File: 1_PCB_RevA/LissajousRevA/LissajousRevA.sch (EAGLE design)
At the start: 77 parts, among them U101 LM348D, U201 LM348D, U401 LM348D

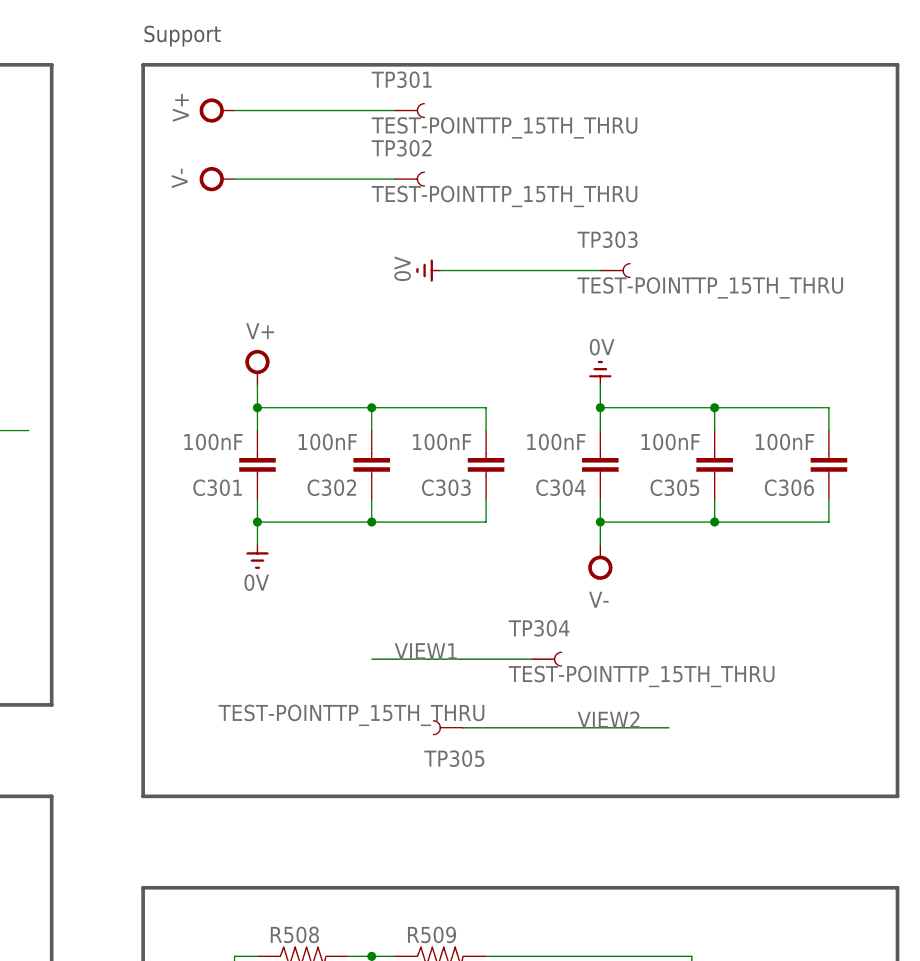
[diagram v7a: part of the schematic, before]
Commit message: added bigger test pads to pcb
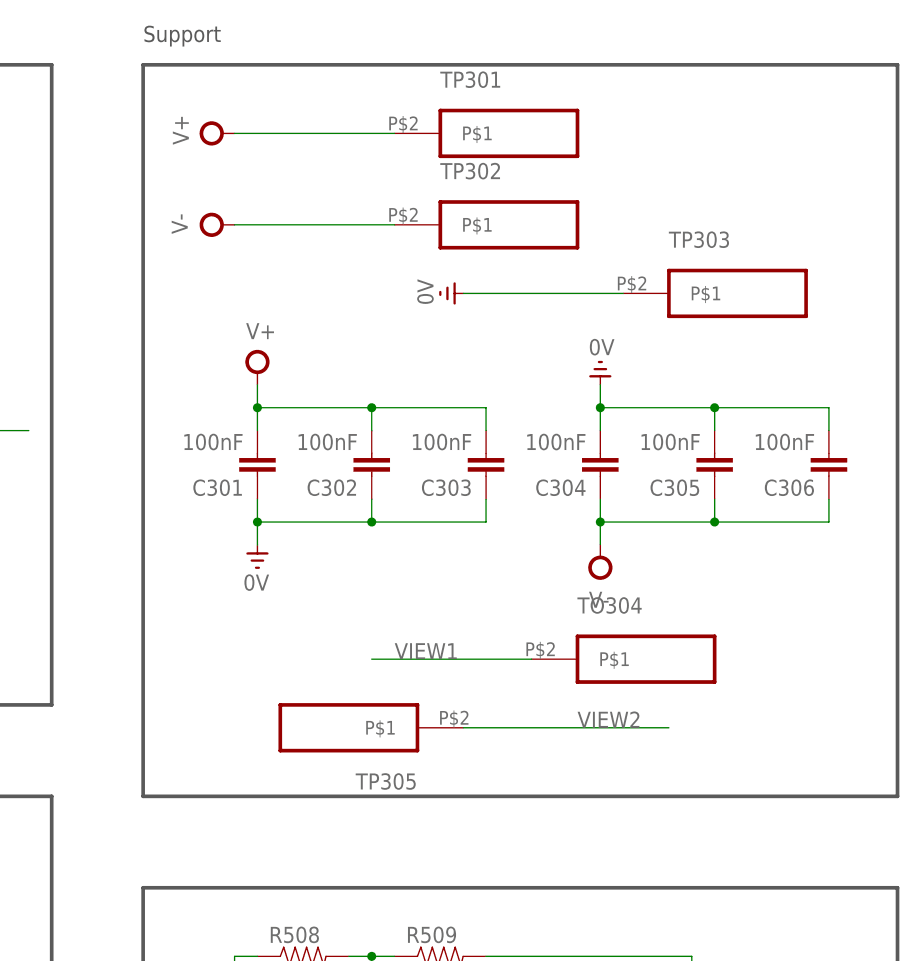
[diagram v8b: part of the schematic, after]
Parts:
- removed TP304: TEST-POINTTP_15TH_THRU, passives:TEST-POINTTP_15TH_THRU
- added TO304: PAD, pad:PAD
- TP301, TP302, TP303, TP305: value TEST-POINTTP_15TH_THRU -> PAD; device passives:TEST-POINTTP_15TH_THRU -> pad:PAD
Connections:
- net 0V: now also TP303.P$1; no longer TP303.1
- net V+: now also TP301.P$1; no longer TP301.1
- net V-: now also TP302.P$1; no longer TP302.1
- net VIEW1: now also TO304.P$1; no longer TP304.1
- net VIEW2: now also TP305.P$1; no longer TP305.1
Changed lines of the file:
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@@
 <part name="R206" library="passives" deviceset="RESISTOR" device="0603-RES" value="0R"/>
 <part name="R209" library="passives" deviceset="RESISTOR" device="0603-RES" value="0R"/>
-<part name="TP301" library="passives" deviceset="TEST-POINT" device="TP_15TH_THRU"/>
-<part name="TP303" library="passives" deviceset="TEST-POINT" device="TP_15TH_THRU"/>
 <part name="C301" library="passives" deviceset="CAP" device="0603-CAP" value="100nF"/>
 <part name="C302" library="passives" deviceset="CAP" device="0603-CAP" value="100nF"/>
@@
 <part name="V12" library="supply" deviceset="V+" device=""/>
 <part name="V13" library="supply" deviceset="V-" device=""/>
-<part name="TP302" library="passives" deviceset="TEST-POINT" device="TP_15TH_THRU"/>
 <part name="C303" library="passives" deviceset="CAP" device="0603-CAP" value="100nF"/>
 <part name="C304" library="passives" deviceset="CAP" device="0603-CAP" value="100nF"/>
@@
 <part name="R510" library="passives" deviceset="RESISTOR" device="0603-RES" value="33K"/>
 <part name="V31" library="supply" deviceset="0V" device=""/>
-<part name="TP305" library="passives" deviceset="TEST-POINT" device="TP_15TH_THRU"/>
-<part name="TP304" library="passives" deviceset="TEST-POINT" device="TP_15TH_THRU"/>
 <part name="C506" library="passives" deviceset="CAP" device="0603-CAP" value="10nF"/>
+<part name="TP301" library="pad" deviceset="PAD" device=""/>
+<part name="TP302" library="pad" deviceset="PAD" device=""/>
+<part name="TP303" library="pad" deviceset="PAD" device=""/>
+<part name="TO304" library="pad" deviceset="PAD" device=""/>
+<part name="TP305" library="pad" deviceset="PAD" device=""/>
 </parts>
 <sheets>
@@
 <instance part="R206" gate="G$1" x="83.82" y="127" rot="R180"/>
 <instance part="R209" gate="G$1" x="170.18" y="127" rot="R180"/>
-<instance part="TP301" gate="G$1" x="317.5" y="243.84"/>
-<instance part="TP303" gate="G$1" x="340.36" y="226.06"/>
 <instance part="C301" gate="G$1" x="302.26" y="205.74" rot="R180"/>
 <instance part="C302" gate="G$1" x="314.96" y="205.74" rot="R180"/>
-<instance part="V11" gate="1" x="320.04" y="226.06" rot="R270"/>
-<instance part="V12" gate="1" x="297.18" y="243.84" rot="R90"/>
-<instance part="V13" gate="1" x="297.18" y="236.22" rot="R270"/>
-<instance part="TP302" gate="G$1" x="317.5" y="236.22"/>
+<instance part="V11" gate="1" x="322.58" y="223.52" rot="R270"/>
+<instance part="V12" gate="1" x="297.18" y="241.3" rot="R90"/>
+<instance part="V13" gate="1" x="297.18" y="231.14" rot="R270"/>
 <instance part="C303" gate="G$1" x="327.66" y="205.74" rot="R180"/>
 <instance part="C304" gate="G$1" x="340.36" y="205.74" rot="R180"/>
@@
 <instance part="R510" gate="G$1" x="350.52" y="109.22" rot="R90"/>
 <instance part="V31" gate="1" x="350.52" y="99.06"/>
+<instance part="C506" gate="G$1" x="350.52" y="121.92"/>
+<instance part="TP301" gate="G$1" x="317.5" y="241.3"/>
+<instance part="TP302" gate="G$1" x="317.5" y="231.14"/>
+<instance part="TP303" gate="G$1" x="342.9" y="223.52"/>
+<instance part="TO304" gate="G$1" x="332.74" y="182.88"/>
 <instance part="TP305" gate="G$1" x="325.12" y="175.26" rot="R180"/>
-<instance part="TP304" gate="G$1" x="332.74" y="182.88"/>
-<instance part="C506" gate="G$1" x="350.52" y="121.92"/>
 </instances>
 <busses>
@@
 </segment>
 <segment>
-<pinref part="TP302" gate="G$1" pin="1"/>
-<wire x1="317.5" y1="236.22" x2="299.72" y2="236.22" width="0.1524" layer="91"/>
+<wire x1="317.5" y1="231.14" x2="299.72" y2="231.14" width="0.1524" layer="91"/>
 <pinref part="V13" gate="1" pin="V-"/>
+<pinref part="TP302" gate="G$1" pin="P$1"/>
 </segment>
 <segment>
@@
 </segment>
 <segment>
-<pinref part="TP301" gate="G$1" pin="1"/>
 <pinref part="V12" gate="1" pin="V+"/>
-<wire x1="317.5" y1="243.84" x2="299.72" y2="243.84" width="0.1524" layer="91"/>
+<wire x1="317.5" y1="241.3" x2="299.72" y2="241.3" width="0.1524" layer="91"/>
+<pinref part="TP301" gate="G$1" pin="P$1"/>
 </segment>
 <segment>
@@
 </segment>
 <segment>
-<pinref part="TP303" gate="G$1" pin="1"/>
-<wire x1="340.36" y1="226.06" x2="322.58" y2="226.06" width="0.1524" layer="91"/>
+<wire x1="342.9" y1="223.52" x2="325.12" y2="223.52" width="0.1524" layer="91"/>
 <pinref part="V11" gate="1" pin="0V"/>
+<pinref part="TP303" gate="G$1" pin="P$1"/>
 </segment>
 <segment>
@@
 </segment>
 <segment>
-<pinref part="TP304" gate="G$1" pin="1"/>
 <wire x1="332.74" y1="182.88" x2="314.96" y2="182.88" width="0.1524" layer="91"/>
 <label x="317.5" y="182.88" size="1.778" layer="95"/>
+<pinref part="TO304" gate="G$1" pin="P$1"/>
 </segment>
 </net>
@@
 </segment>
 <segment>
-<pinref part="TP305" gate="G$1" pin="1"/>
 <wire x1="325.12" y1="175.26" x2="347.98" y2="175.26" width="0.1524" layer="91"/>
 <label x="337.82" y="175.26" size="1.778" layer="95"/>
-</segment>
-</net>
+<pinref part="TP305" gate="G$1" pin="P$1"/>
+</segment>
+</net>
